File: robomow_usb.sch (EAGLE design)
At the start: 25 parts, among them IC1 FT231XS-R, J1 RJ11-2L-B, U1 SN65HVD1176

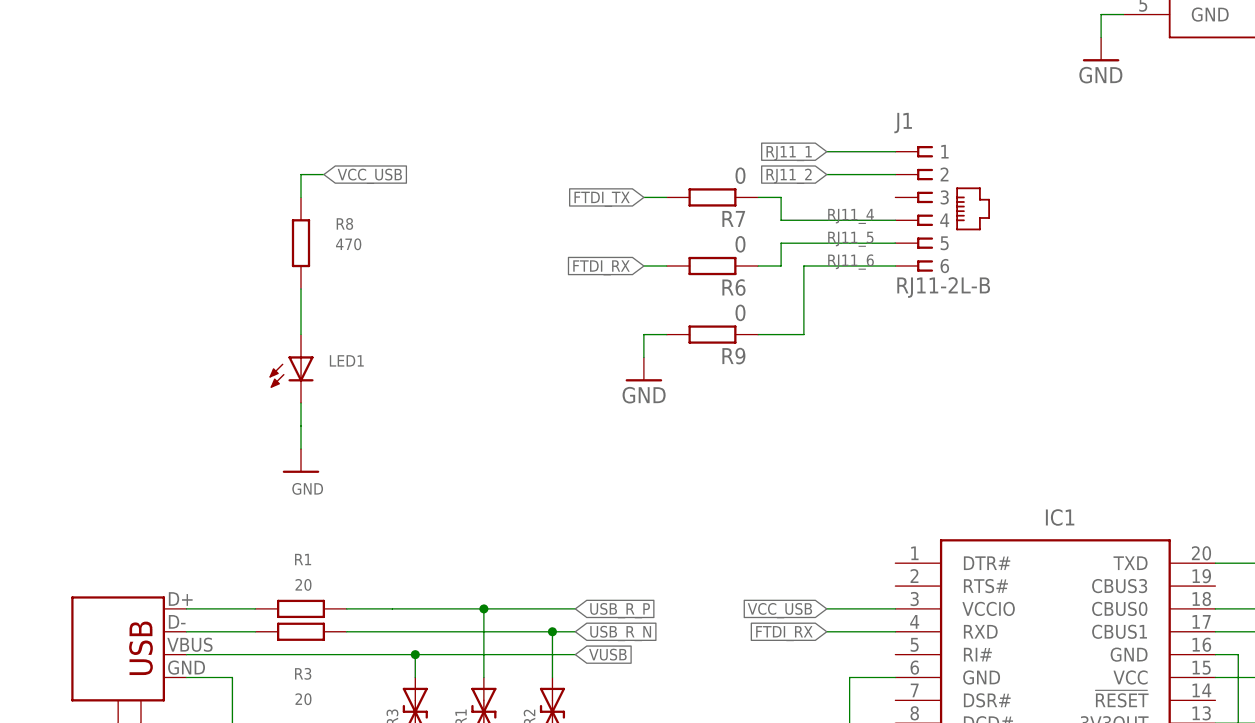
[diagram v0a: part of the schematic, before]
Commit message: Added TX RX LEDs
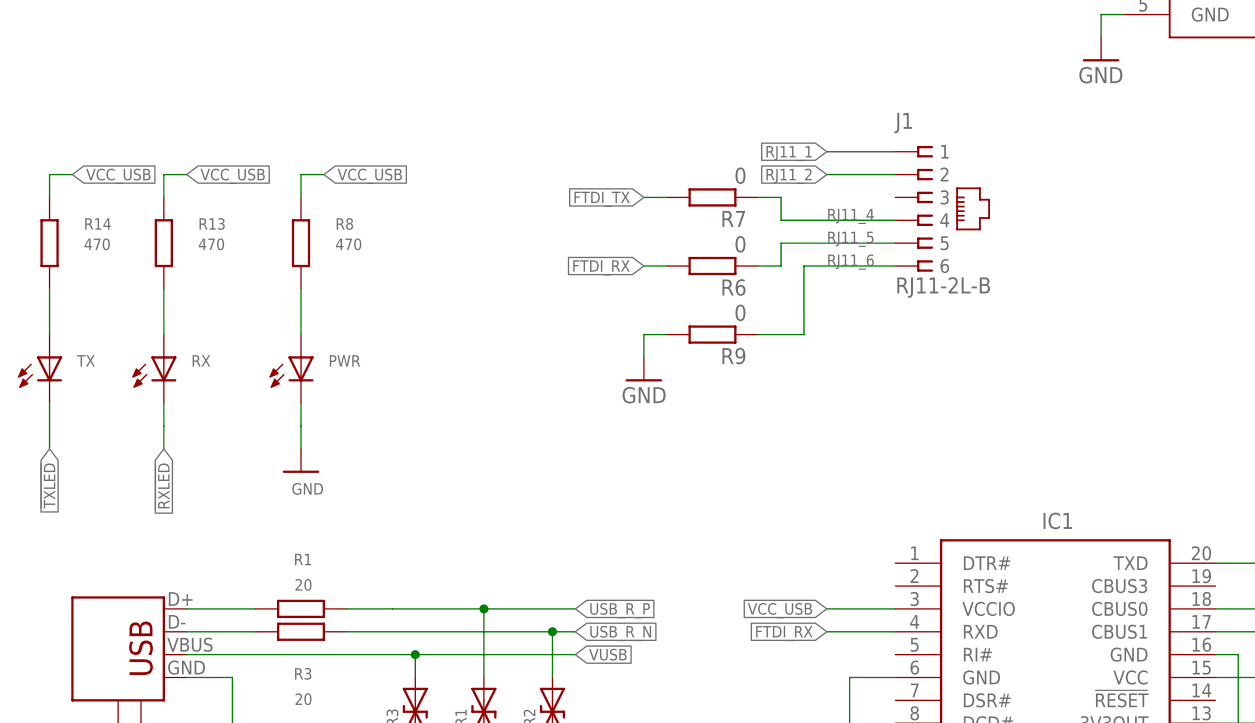
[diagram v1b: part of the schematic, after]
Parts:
- added R13, R14: 470, rcl:R-EU_R0603
- added RX, TX: (no value), dp_devices:LED-0603
- renumbered LED1 to PWR
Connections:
- new net VIN_LED_R2: R13.2, RX.A
- new net VIN_LED_R3: R14.2, TX.A
- net !RXLED: now also RX.C
- net !TXLED: now also TX.C
- net VCC_USB: now also R13.1, R14.1
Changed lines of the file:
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@@
 <?xml version="1.0" encoding="utf-8"?>
 <!DOCTYPE eagle SYSTEM "eagle.dtd">
-<eagle version="9.5.2">
+<eagle version="9.6.2">
 <drawing>
 <settings>
@@
 <part name="GND9" library="supply1" deviceset="GND" device=""/>
 <part name="P+2" library="SparkFun" deviceset="3.3V" device=""/>
-<part name="LED1" library="dp_devices" deviceset="LED" device="-0603"/>
+<part name="PWR" library="dp_devices" deviceset="LED" device="-0603"/>
 <part name="R8" library="rcl" deviceset="R-EU_" device="R0603" value="470">
 <attribute name="OC_TME" value="0603SAF1001T5E"/>
@@
 </part>
 <part name="FRAME1" library="martonmiklos" deviceset="A4L-LOC" device=""/>
+<part name="RX" library="dp_devices" deviceset="LED" device="-0603"/>
+<part name="R13" library="rcl" deviceset="R-EU_" device="R0603" value="470">
+<attribute name="OC_TME" value="0603SAF1001T5E"/>
+</part>
+<part name="TX" library="dp_devices" deviceset="LED" device="-0603"/>
+<part name="R14" library="rcl" deviceset="R-EU_" device="R0603" value="470">
+<attribute name="OC_TME" value="0603SAF1001T5E"/>
+</part>
 </parts>
 <sheets>
@@
 </instance>
 <instance part="IC1" gate="G$1" x="132.08" y="50.8" smashed="yes">
-<attribute name="NAME" x="130.81" y="68.58" size="1.778" layer="95" align="center-left"/>
+<attribute name="NAME" x="132.334" y="67.31" size="1.778" layer="95" align="bottom-center"/>
 <attribute name="VALUE" x="120.65" y="35.56" size="1.778" layer="96" align="center-left"/>
 </instance>
@@
 <attribute name="VALUE" x="176.784" y="72.136" size="1.778" layer="96"/>
 </instance>
-<instance part="LED1" gate="LED" x="48.26" y="86.36" smashed="yes">
+<instance part="PWR" gate="LED" x="48.26" y="86.36" smashed="yes">
 <attribute name="NAME" x="51.308" y="85.344" size="1.27" layer="95" font="vector" ratio="10"/>
 <attribute name="VALUE" x="53.975" y="81.788" size="1.778" layer="96" rot="R90"/>
@@
 <attribute name="SHEET" x="230.505" y="5.08" size="2.54" layer="94" font="vector"/>
 <attribute name="SHEET_HEADLINE" x="162.56" y="20.32" size="1.778" layer="94" font="vector"/>
+</instance>
+<instance part="RX" gate="LED" x="33.02" y="86.36" smashed="yes">
+<attribute name="NAME" x="36.068" y="85.344" size="1.27" layer="95" font="vector" ratio="10"/>
+<attribute name="VALUE" x="38.735" y="81.788" size="1.778" layer="96" rot="R90"/>
+</instance>
+<instance part="R13" gate="G$1" x="33.02" y="99.06" smashed="yes" rot="R270">
+<attribute name="NAME" x="36.83" y="100.5586" size="1.27" layer="95" font="vector" ratio="10"/>
+<attribute name="VALUE" x="36.83" y="98.298" size="1.27" layer="96" font="vector" ratio="10"/>
+<attribute name="OC_TME" x="33.02" y="99.06" size="1.778" layer="96" rot="R270" display="off"/>
+</instance>
+<instance part="TX" gate="LED" x="20.32" y="86.36" smashed="yes">
+<attribute name="NAME" x="23.368" y="85.344" size="1.27" layer="95" font="vector" ratio="10"/>
+<attribute name="VALUE" x="26.035" y="81.788" size="1.778" layer="96" rot="R90"/>
+</instance>
+<instance part="R14" gate="G$1" x="20.32" y="99.06" smashed="yes" rot="R270">
+<attribute name="NAME" x="24.13" y="100.5586" size="1.27" layer="95" font="vector" ratio="10"/>
+<attribute name="VALUE" x="24.13" y="98.298" size="1.27" layer="96" font="vector" ratio="10"/>
+<attribute name="OC_TME" x="20.32" y="99.06" size="1.778" layer="96" rot="R270" display="off"/>
 </instance>
 </instances>
@@
 <segment>
 <wire x1="48.26" y1="76.2" x2="48.26" y2="78.74" width="0.1524" layer="91"/>
-<pinref part="LED1" gate="LED" pin="C"/>
+<pinref part="PWR" gate="LED" pin="C"/>
 <wire x1="48.26" y1="78.74" x2="48.26" y2="81.28" width="0.1524" layer="91"/>
 <pinref part="GND2" gate="1" pin="GND"/>
@@
 <label x="129.54" y="144.78" size="1.27" layer="95" font="vector" rot="R180" xref="yes"/>
 </segment>
+<segment>
+<pinref part="R13" gate="G$1" pin="1"/>
+<wire x1="33.02" y1="104.14" x2="33.02" y2="106.68" width="0.1524" layer="91"/>
+<wire x1="33.02" y1="106.68" x2="35.56" y2="106.68" width="0.1524" layer="91"/>
+<label x="35.56" y="106.68" size="1.27" layer="95" font="vector" xref="yes"/>
+</segment>
+<segment>
+<pinref part="R14" gate="G$1" pin="1"/>
+<wire x1="20.32" y1="104.14" x2="20.32" y2="106.68" width="0.1524" layer="91"/>
+<wire x1="20.32" y1="106.68" x2="22.86" y2="106.68" width="0.1524" layer="91"/>
+<label x="22.86" y="106.68" size="1.27" layer="95" font="vector" xref="yes"/>
+</segment>
 </net>
 <net name="FTDI_TX" class="0">
@@
 <net name="VIN_LED_R1" class="0">
 <segment>
-<pinref part="LED1" gate="LED" pin="A"/>
+<pinref part="PWR" gate="LED" pin="A"/>
 <pinref part="R8" gate="G$1" pin="2"/>
 <wire x1="48.26" y1="88.9" x2="48.26" y2="93.98" width="0.1524" layer="91"/>
@@
 <label x="160.02" y="55.88" size="1.27" layer="95" font="vector" xref="yes"/>
 </segment>
+<segment>
+<wire x1="33.02" y1="76.2" x2="33.02" y2="78.74" width="0.1524" layer="91"/>
+<pinref part="RX" gate="LED" pin="C"/>
+<wire x1="33.02" y1="78.74" x2="33.02" y2="81.28" width="0.1524" layer="91"/>
+<label x="33.02" y="76.2" size="1.27" layer="95" rot="R270" xref="yes"/>
+</segment>
 </net>
 <net name="!TXLED" class="0">
@@
 <wire x1="114.3" y1="40.64" x2="106.68" y2="40.64" width="0.1524" layer="91"/>
 <label x="106.68" y="40.64" size="1.27" layer="95" font="vector" rot="R180" xref="yes"/>
+</segment>
+<segment>
+<wire x1="20.32" y1="76.2" x2="20.32" y2="78.74" width="0.1524" layer="91"/>
+<pinref part="TX" gate="LED" pin="C"/>
+<wire x1="20.32" y1="78.74" x2="20.32" y2="81.28" width="0.1524" layer="91"/>
+<label x="20.32" y="76.2" size="1.27" layer="95" rot="R270" xref="yes"/>
 </segment>
 </net>
@@
 </segment>
 </net>
+<net name="VIN_LED_R2" class="0">
+<segment>
+<pinref part="RX" gate="LED" pin="A"/>
+<pinref part="R13" gate="G$1" pin="2"/>
+<wire x1="33.02" y1="88.9" x2="33.02" y2="93.98" width="0.1524" layer="91"/>
+</segment>
+</net>
+<net name="VIN_LED_R3" class="0">
+<segment>
+<pinref part="TX" gate="LED" pin="A"/>
+<pinref part="R14" gate="G$1" pin="2"/>
+<wire x1="20.32" y1="88.9" x2="20.32" y2="93.98" width="0.1524" layer="91"/>
+</segment>
+</net>

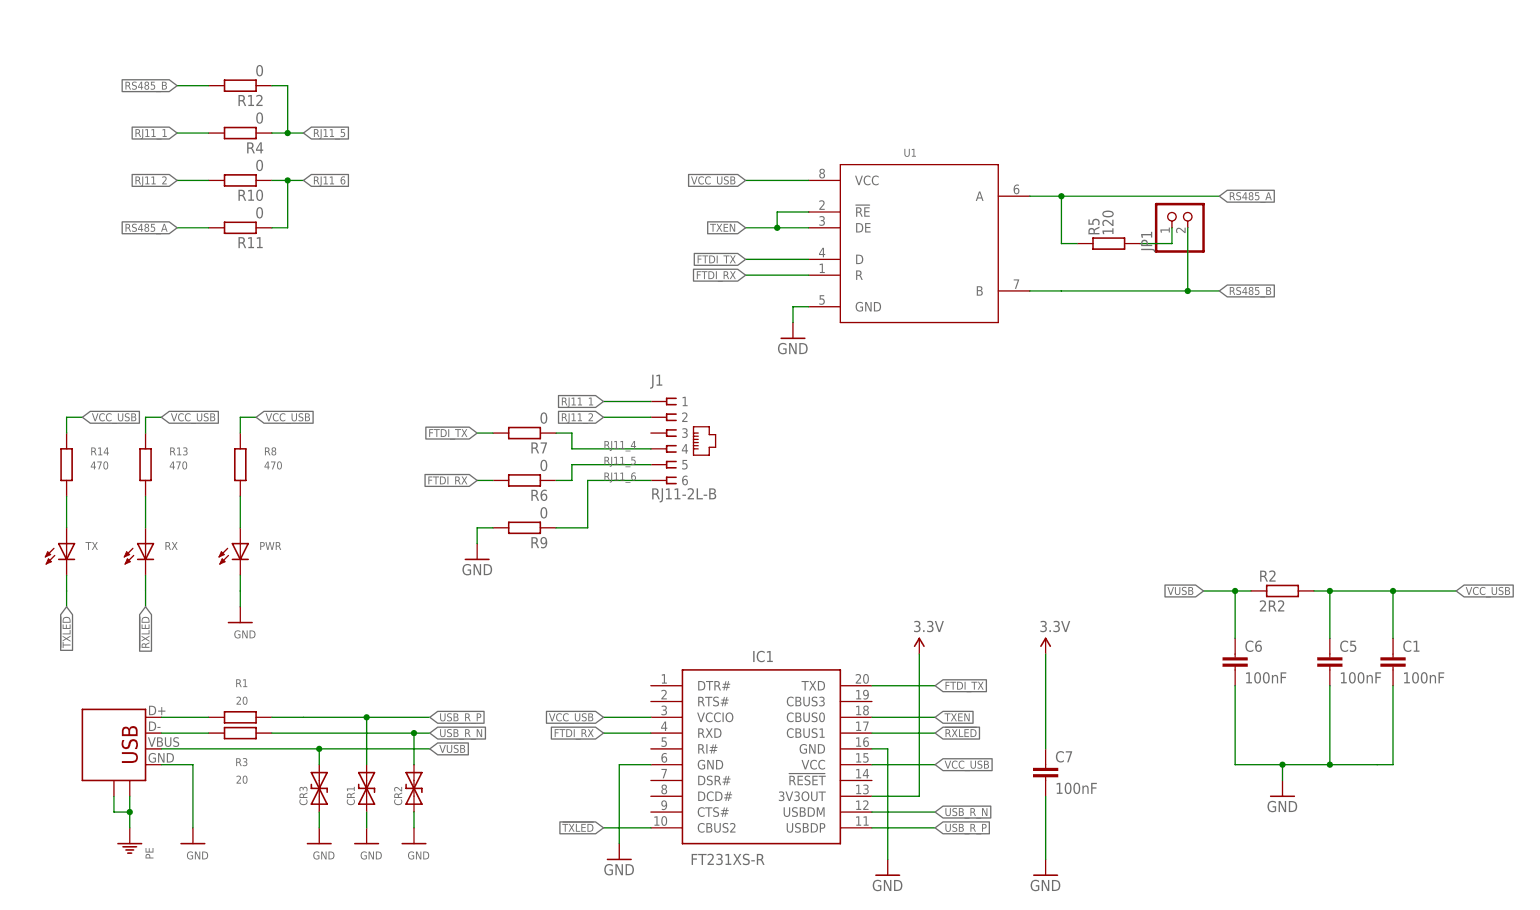
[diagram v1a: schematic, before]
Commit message: Full pass on DRC (removed stubs)
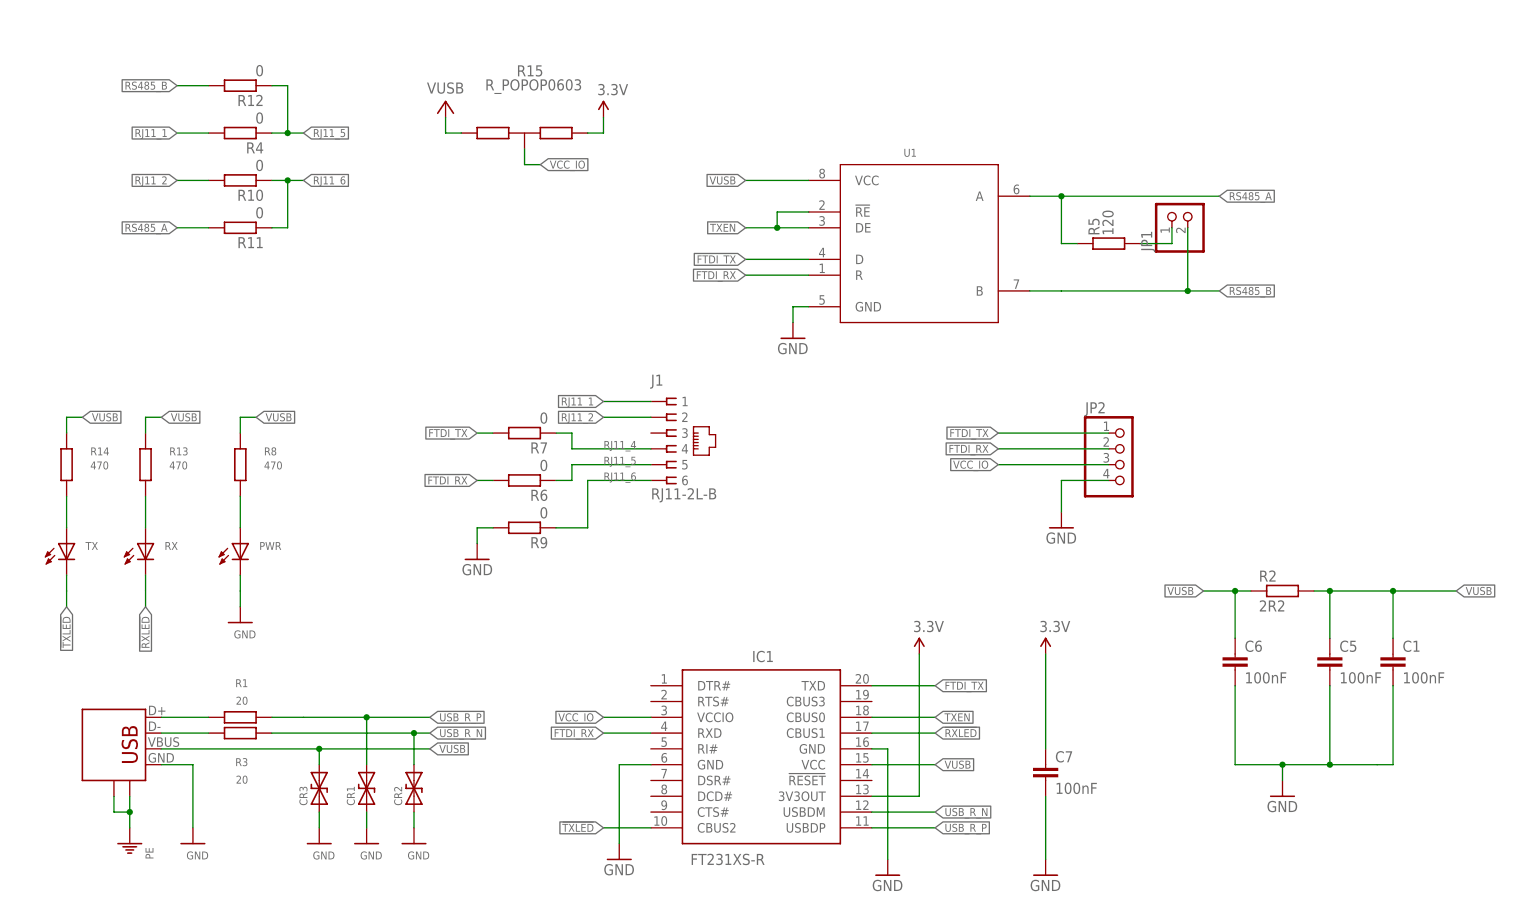
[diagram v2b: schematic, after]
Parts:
- added JP2: (no value), pinhead:PINHD-1X4
- added R15: R_POPOP0603, martonmiklos:R_POPOP0603
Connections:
- removed net VCC_USB: C1.1, C5.1, IC1.VCC, IC1.VCCIO, R13.1, R14.1, R2.2, R8.1, U1.VCC
- new net VCC_IO: IC1.VCCIO, JP2.3, R15.COM
- net 3.3V: now also R15.A
- net FTDI_RX: now also JP2.2
- net FTDI_TX: now also JP2.1
- net GND: now also JP2.4
- net VUSB: now also C1.1, C5.1, IC1.VCC, R13.1, R14.1, R15.B, R2.2, R8.1, U1.VCC
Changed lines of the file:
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@@
 <attribute name="OC_TME" value="0603SAF1001T5E"/>
 </part>
+<part name="JP2" library="pinhead" deviceset="PINHD-1X4" device=""/>
+<part name="GND6" library="supply1" deviceset="GND" device=""/>
+<part name="R15" library="martonmiklos" deviceset="R_POPOP" device="0603"/>
+<part name="P+3" library="SparkFun" deviceset="3.3V" device=""/>
+<part name="P+4" library="supply1" deviceset="VUSB" device=""/>
 </parts>
 <sheets>
@@
 <attribute name="VALUE" x="24.13" y="98.298" size="1.27" layer="96" font="vector" ratio="10"/>
 <attribute name="OC_TME" x="20.32" y="99.06" size="1.778" layer="96" rot="R270" display="off"/>
+</instance>
+<instance part="JP2" gate="A" x="190.5" y="99.06" smashed="yes">
+<attribute name="NAME" x="184.15" y="107.315" size="1.778" layer="95"/>
+<attribute name="VALUE" x="184.15" y="91.44" size="1.778" layer="96"/>
+</instance>
+<instance part="GND6" gate="1" x="180.34" y="88.9" smashed="yes">
+<attribute name="VALUE" x="177.8" y="86.36" size="1.778" layer="96"/>
+</instance>
+<instance part="R15" gate="G$1" x="93.98" y="152.4" smashed="yes" rot="R90">
+<attribute name="NAME" x="92.71" y="161.5186" size="1.778" layer="95"/>
+<attribute name="VALUE" x="87.63" y="159.258" size="1.778" layer="96"/>
+</instance>
+<instance part="P+3" gate="G$1" x="106.68" y="154.94" smashed="yes">
+<attribute name="VALUE" x="105.664" y="158.496" size="1.778" layer="96"/>
+</instance>
+<instance part="P+4" gate="G$1" x="81.28" y="157.48" smashed="yes">
+<attribute name="VALUE" x="81.28" y="158.75" size="1.778" layer="96" align="bottom-center"/>
 </instance>
 </instances>
@@
 <wire x1="86.36" y1="88.9" x2="86.36" y2="86.36" width="0.1524" layer="91"/>
 </segment>
+<segment>
+<pinref part="JP2" gate="A" pin="4"/>
+<wire x1="187.96" y1="96.52" x2="180.34" y2="96.52" width="0.1524" layer="91"/>
+<pinref part="GND6" gate="1" pin="GND"/>
+<wire x1="180.34" y1="96.52" x2="180.34" y2="91.44" width="0.1524" layer="91"/>
+</segment>
 </net>
 <net name="USB_R_N" class="0">
@@
 <label x="203.2" y="78.74" size="1.27" layer="95" font="vector" rot="R180" xref="yes"/>
 </segment>
-</net>
-<net name="USB_N" class="5">
-<segment>
-<pinref part="JUSB" gate="G$1" pin="D-"/>
-<pinref part="R3" gate="G$1" pin="2"/>
-<wire x1="43.18" y1="55.88" x2="35.56" y2="55.88" width="0.1524" layer="91"/>
-</segment>
-</net>
-<net name="USB_P" class="4">
-<segment>
-<pinref part="JUSB" gate="G$1" pin="D+"/>
-<pinref part="R1" gate="G$1" pin="2"/>
-<wire x1="43.18" y1="58.42" x2="35.56" y2="58.42" width="0.1524" layer="91"/>
-</segment>
-</net>
-<net name="3.3V" class="0">
-<segment>
-<pinref part="IC1" gate="G$1" pin="3V3OUT"/>
-<pinref part="P+1" gate="G$1" pin="3.3V"/>
-<wire x1="149.86" y1="45.72" x2="157.48" y2="45.72" width="0.1524" layer="91"/>
-<wire x1="157.48" y1="45.72" x2="157.48" y2="68.58" width="0.1524" layer="91"/>
-</segment>
-<segment>
-<pinref part="P+2" gate="G$1" pin="3.3V"/>
-<pinref part="C7" gate="G$1" pin="1"/>
-<wire x1="177.8" y1="68.58" x2="177.8" y2="53.34" width="0.1524" layer="91"/>
-</segment>
-</net>
-<net name="VCC_USB" class="0">
-<segment>
-<pinref part="IC1" gate="G$1" pin="VCCIO"/>
-<wire x1="114.3" y1="58.42" x2="106.68" y2="58.42" width="0.1524" layer="91"/>
-<label x="106.68" y="58.42" size="1.27" layer="95" font="vector" rot="R180" xref="yes"/>
+<segment>
+<pinref part="R15" gate="G$1" pin="B"/>
+<wire x1="83.82" y1="152.4" x2="81.28" y2="152.4" width="0.1524" layer="91"/>
+<pinref part="P+4" gate="G$1" pin="VUSB"/>
+<wire x1="81.28" y1="152.4" x2="81.28" y2="154.94" width="0.1524" layer="91"/>
 </segment>
 <segment>
@@
 </segment>
 </net>
+<net name="USB_N" class="5">
+<segment>
+<pinref part="JUSB" gate="G$1" pin="D-"/>
+<pinref part="R3" gate="G$1" pin="2"/>
+<wire x1="43.18" y1="55.88" x2="35.56" y2="55.88" width="0.1524" layer="91"/>
+</segment>
+</net>
+<net name="USB_P" class="4">
+<segment>
+<pinref part="JUSB" gate="G$1" pin="D+"/>
+<pinref part="R1" gate="G$1" pin="2"/>
+<wire x1="43.18" y1="58.42" x2="35.56" y2="58.42" width="0.1524" layer="91"/>
+</segment>
+</net>
+<net name="3.3V" class="0">
+<segment>
+<pinref part="IC1" gate="G$1" pin="3V3OUT"/>
+<pinref part="P+1" gate="G$1" pin="3.3V"/>
+<wire x1="149.86" y1="45.72" x2="157.48" y2="45.72" width="0.1524" layer="91"/>
+<wire x1="157.48" y1="45.72" x2="157.48" y2="68.58" width="0.1524" layer="91"/>
+</segment>
+<segment>
+<pinref part="P+2" gate="G$1" pin="3.3V"/>
+<pinref part="C7" gate="G$1" pin="1"/>
+<wire x1="177.8" y1="68.58" x2="177.8" y2="53.34" width="0.1524" layer="91"/>
+</segment>
+<segment>
+<pinref part="R15" gate="G$1" pin="A"/>
+<wire x1="104.14" y1="152.4" x2="106.68" y2="152.4" width="0.1524" layer="91"/>
+<pinref part="P+3" gate="G$1" pin="3.3V"/>
+<wire x1="106.68" y1="152.4" x2="106.68" y2="154.94" width="0.1524" layer="91"/>
+</segment>
+</net>
 <net name="FTDI_TX" class="0">
 <segment>
@@
 <pinref part="R7" gate="G$1" pin="2"/>
 </segment>
+<segment>
+<pinref part="JP2" gate="A" pin="1"/>
+<wire x1="187.96" y1="104.14" x2="170.18" y2="104.14" width="0.1524" layer="91"/>
+<label x="170.18" y="104.14" size="1.27" layer="95" font="vector" rot="R180" xref="yes"/>
+</segment>
 </net>
 <net name="FTDI_RX" class="0">
@@
 <label x="86.36" y="96.52" size="1.27" layer="95" font="vector" rot="MR0" xref="yes"/>
 <pinref part="R6" gate="G$1" pin="2"/>
+</segment>
+<segment>
+<pinref part="JP2" gate="A" pin="2"/>
+<wire x1="187.96" y1="101.6" x2="170.18" y2="101.6" width="0.1524" layer="91"/>
+<label x="170.18" y="101.6" size="1.27" layer="95" font="vector" rot="R180" xref="yes"/>
 </segment>
 </net>
@@
 </segment>
 </net>
+<net name="VCC_IO" class="0">
+<segment>
+<pinref part="R15" gate="G$1" pin="COM"/>
+<wire x1="93.98" y1="149.86" x2="93.98" y2="147.32" width="0.1524" layer="91"/>
+<wire x1="93.98" y1="147.32" x2="96.52" y2="147.32" width="0.1524" layer="91"/>
+<label x="96.52" y="147.32" size="1.27" layer="95" font="vector" xref="yes"/>
+</segment>
+<segment>
+<pinref part="IC1" gate="G$1" pin="VCCIO"/>
+<wire x1="114.3" y1="58.42" x2="106.68" y2="58.42" width="0.1524" layer="91"/>
+<label x="106.68" y="58.42" size="1.27" layer="95" font="vector" rot="R180" xref="yes"/>
+</segment>
+<segment>
+<pinref part="JP2" gate="A" pin="3"/>
+<wire x1="187.96" y1="99.06" x2="170.18" y2="99.06" width="0.1524" layer="91"/>
+<label x="170.18" y="99.06" size="1.27" layer="95" font="vector" rot="R180" xref="yes"/>
+</segment>
+</net>
 </nets>
 </sheet>
 </sheets>
+<errors>
+</errors>
 </schematic>
 </drawing>
